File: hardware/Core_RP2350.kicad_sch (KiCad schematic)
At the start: 79 parts, among them J19 Micro_SD_Card_Det_Hirose_DM3AT, J20 USB_C_Receptacle_USB2.0, J21 5-146281-3, J22 5-146281-3, J4 AudioJack3, SW1 SPST-NO, SW2 SPST-NO, SW3 SPST-NO, U1 RP2350B-QFN80, U2 ADUM4160, U3 W25Q128JVS

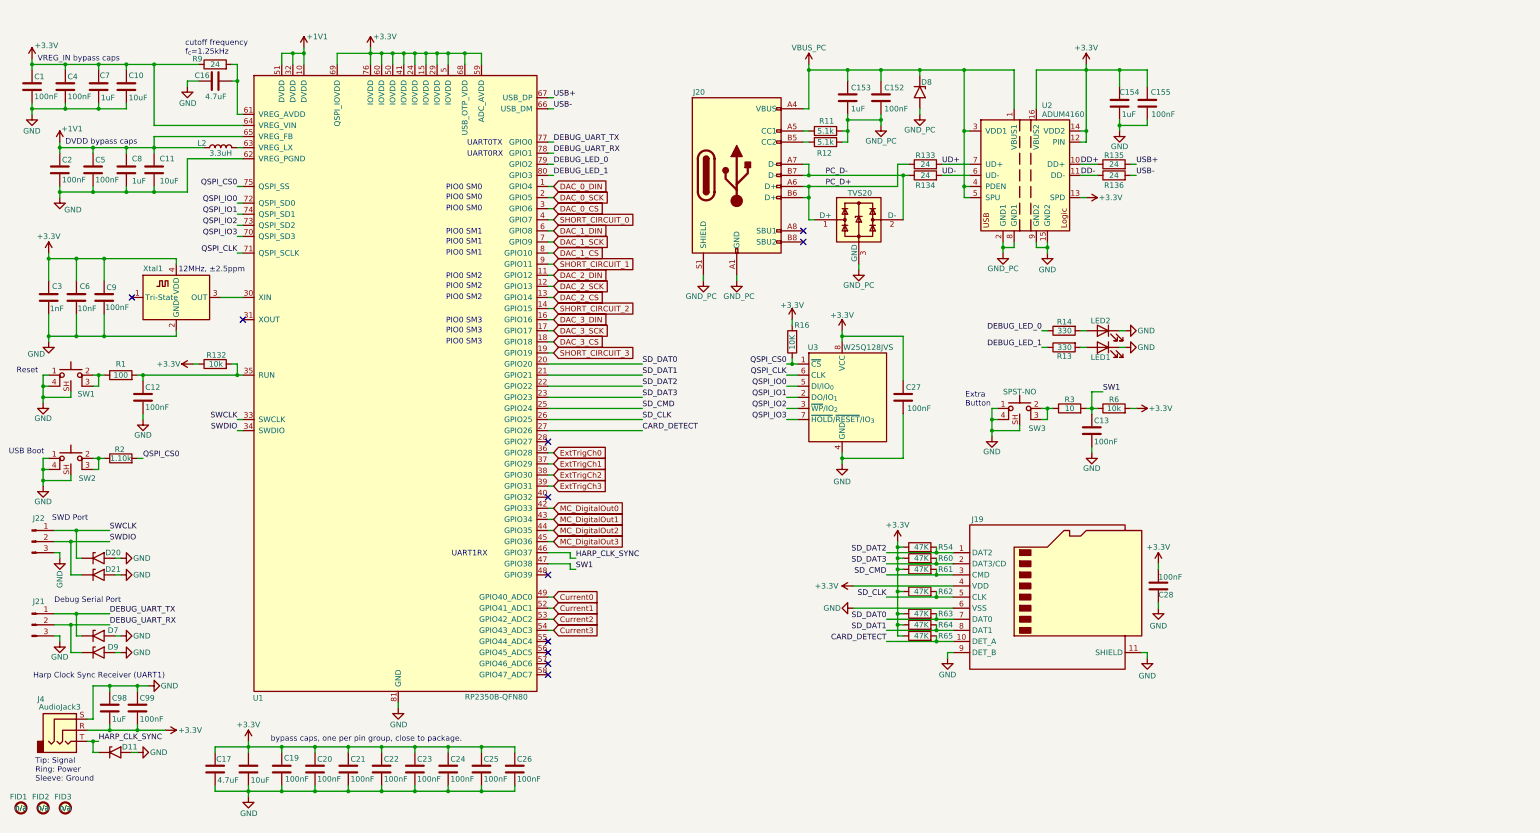
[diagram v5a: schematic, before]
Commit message: update short detection; draft bom
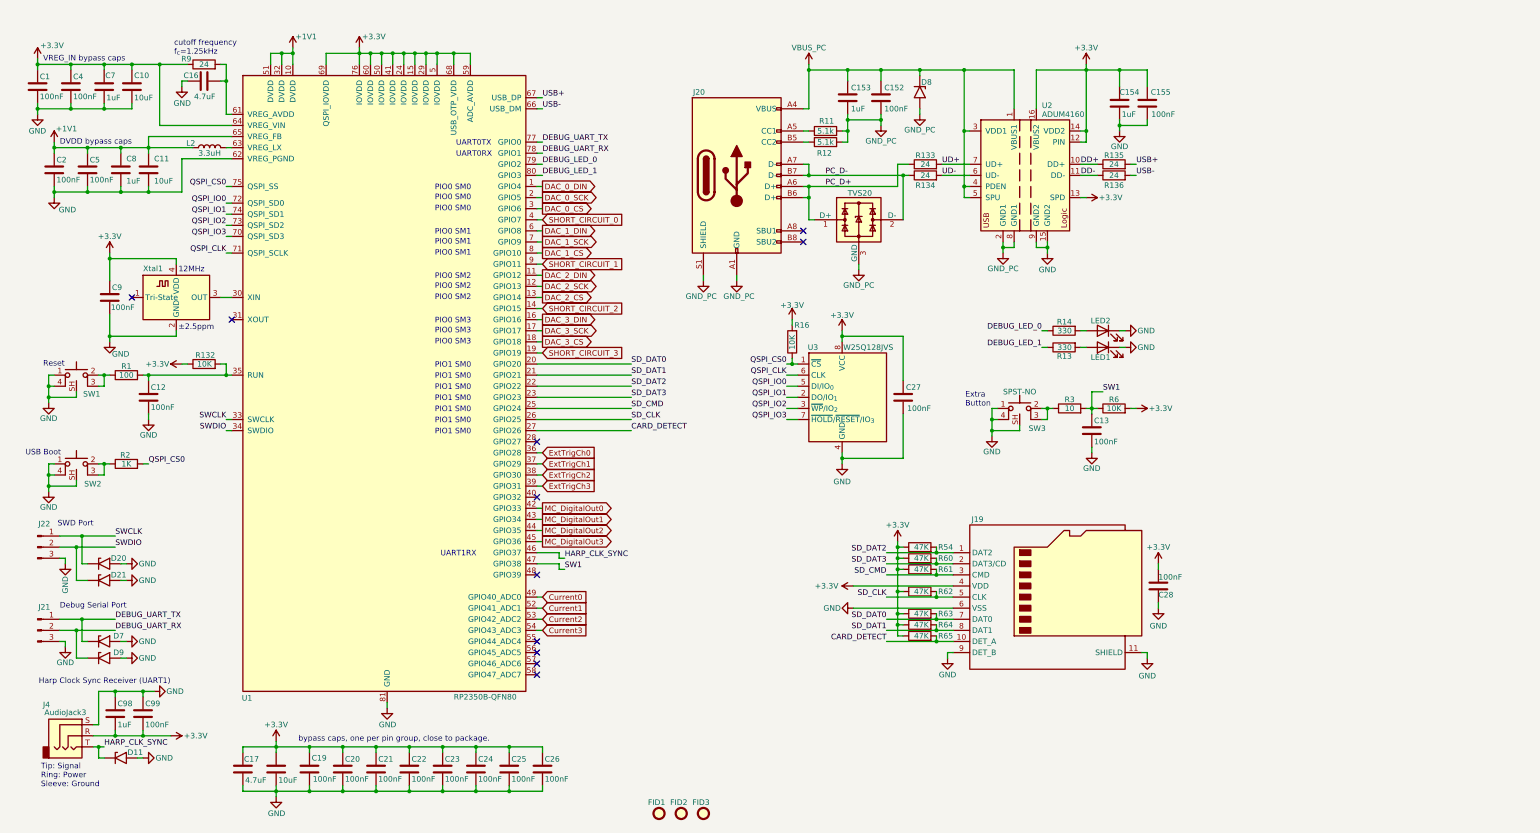
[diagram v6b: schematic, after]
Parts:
- removed C3: 1nF, Capacitor_SMD:C_0603_1608Metric, symbol harp.device.quad.dac:C_0603
- removed C6: 10nF, Capacitor_SMD:C_0603_1608Metric, symbol harp.device.quad.dac:C_0603
- C1, C12, C13, C152, C155, C19, C2, C20, C21, C22, C23, C24, C25, C26, C27, C28, C4, C5, C9, C99: footprint Capacitor_SMD:C_0603_1608Metric -> Capacitor_SMD:C_0402_1005Metric; Link https://www.digikey.com/en/products/detail/kemet/C0603C104K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 -> https://www.digikey.com/en/products/detail/murata-electroni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; Manufacturer KEMET -> Murata Electronics; Manufacturer Number C0603C104K5RACTU -> GRM155R71H104KE14D; Manufacturer_Name KEMET -> (none); Manufacturer_Part_Number C0603C104K5RACTU -> (none); PCBWay Link https://www.pcbway.com/components/detail/0402B104K160CT/307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 -> (none); Temperature Coefficient (none) -> X7R
- C10, C11, C18: Alternate CL21B106KOQNNNE -> (none); Manufacturer_Name Murata Electronics -> (none); Manufacturer_Part_Number GRM188R61E106KA73D -> (none); Temperature Coefficient (none) -> X5R
- C153, C154, C7, C8, C98: Manufacturer_Name TDK -> (none); Manufacturer_Part_Number C1608X7R1H105K080AB -> (none)
- C16, C17: Manufacturer_Name TDK -> (none); Manufacturer_Part_Number C1608X5R1V475K080AC -> (none)
- D11, D20, D21, D7, D8, D9: Link (none) -> https://www.digikey.com/en/products/detail/vishay-general-s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; Manufacturer (none) -> Vishay General Semiconductor - Diodes Division; Manufacturer Number (none) -> VBUS05N1-HD1-G3-08
- FID1, FID2, FID3: Manufacturer_Name n/a -> (none); Manufacturer_Part_Number n/a -> (none)
- J20: Manufacturer_Name JAE Electronics -> (none); Manufacturer_Part_Number DX07S016JA1R1500 -> (none); PCBWay Link https://www.pcbway.com/components/detail/DX07S016JA1R1500/1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 -> (none)
- J21, J22: Manufacturer_Name TE Connectivity -> (none); Manufacturer_Part_Number 5-146281-3 -> (none)
- J4: Manufacturer_Name Same Sky (Formerly CUI Devices) -> (none); Manufacturer_Part_Number SJ-3524-SMT-TR-BE -> (none)
- LED1, LED2: PCBWay Link https://www.pcbway.com/components/detail/XZCDGK53W1VF/50198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 -> (none)
- R1: Manufacturer_Name Yageo -> (none); Manufacturer_Part_Number AC0603FR-13100RL -> (none)
- R11, R12: footprint Resistor_SMD:R_0603_1608Metric -> Resistor_SMD:R_0402_1005Metric; Link https://www.digikey.com/en/products/detail/yageo/RC0603FR-0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 -> (none); Manufacturer Yageo -> (none); Manufacturer Number RT0402FRE075K1L -> (none); Manufacturer_Name Yageo -> (none); Manufacturer_Part_Number RC0603FR-075K1L -> (none); PCBWay Link https://www.pcbway.com/components/detail/RT0402FRE075K1L/44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 -> (none)
- R13, R14: Manufacturer_Name Yageo -> (none); Manufacturer_Part_Number RC0603FR-07330RL -> (none)
- R132: value 10k -> 10K; footprint Resistor_SMD:R_0603_1608Metric -> Resistor_SMD:R_0402_1005Metric; Link https://www.digikey.com/en/products/detail/yageo/RT0603BRD0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 -> (none); Manufacturer Yageo -> (none); Manufacturer Number RC0402FR-07680RL -> (none); Manufacturer_Name Yageo -> (none); Manufacturer_Part_Number RT0603BRD0710KL -> (none)
- R133, R134, R135, R136, R9: Manufacturer_Name Yageo -> (none); Manufacturer_Part_Number AC0603FR-0724RL -> (none)
- R16: footprint Resistor_SMD:R_0603_1608Metric -> Resistor_SMD:R_0402_1005Metric; Link https://www.digikey.com/en/products/detail/yageo/RT0603BRD0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 -> (none); Manufacturer Yageo -> (none); Manufacturer Number RT0402BRD071KL -> (none); Manufacturer_Name Yageo -> (none); Manufacturer_Part_Number RT0603BRD0710KL -> (none)
- R2: value 1.10k -> 1K; footprint Resistor_SMD:R_0603_1608Metric -> Resistor_SMD:R_0402_1005Metric; Link https://www.digikey.com/en/products/detail/yageo/RT0603BRD0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 -> (none); Manufacturer Yageo -> (none); Manufacturer Number RC0402FR-07680RL -> (none); Manufacturer_Name Yageo -> (none); Manufacturer_Part_Number RT0603BRD071K1L -> (none)
- R3: footprint Resistor_SMD:R_0603_1608Metric -> Resistor_SMD:R_0402_1005Metric; Manufacturer Yageo -> (none); Manufacturer Number RT0402BRD071KL -> (none); Manufacturer_Name Yageo -> (none); Manufacturer_Part_Number AC0603FR-1310RL -> (none)
- R54, R60, R61, R62, R63, R64, R65: footprint (none) -> Resistor_SMD:R_0402_1005Metric
- R6: value 10k -> 10K; footprint Resistor_SMD:R_0603_1608Metric -> Resistor_SMD:R_0402_1005Metric; Link https://www.digikey.com/en/products/detail/yageo/RT0603BRD0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 -> (none); Manufacturer Yageo -> (none); Manufacturer Number RT0402BRD071KL -> (none); Manufacturer_Name Yageo -> (none); Manufacturer_Part_Number RT0603BRD0710KL -> (none)
- SW1, SW2, SW3: Manufacturer_Name Würth Elektronik -> (none); Manufacturer_Part_Number 435451019820 -> (none); Supplier Link https://www.digikey.com/en/products/detail/w%C3%BCrth-elekt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 -> (none)
- TVS20: Manufacturer_Name Texas Instruments -> (none); Manufacturer_Part_Number TPD2EUSB30DRTR -> (none); PCBWay Link https://www.pcbway.com/components/detail/TPD2EUSB30ADRTR/32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 -> (none)
- U1: Manufacturer_Name Raspberry Pi -> (none); Manufacturer_Part_Number SC1510-A4 -> (none); Supplier Link https://www.digikey.com/en/products/detail/raspberry-pi/SC1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 -> (none)
- U2: Manufacturer_Name Analog Devices -> (none); Manufacturer_Part_Number ADUM4160BRWZ-RL -> (none); PCBWay Link https://www.pcbway.com/components/detail/ADUM4160BRWZRL/328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 -> (none)
- U3: Manufacturer_Name Winbond Electronics -> (none); Manufacturer_Part_Number W25Q128JVSIQ TR -> (none)
- Xtal1: Manufacturer_Name ECS -> (none); Manufacturer_Part_Number ECS-TXO-2016-33-120-TR -> (none); PCBWay Link https://www.pcbway.com/components/detail/ECSTXO201633120TR/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 -> (none); Supplier Link https://www.digikey.com/en/products/detail/ecs-inc/ECS-TXO-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 -> (none)
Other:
- note added: "12MHz"
- note added: "PIO1 SM0"
- note added: "±2.5ppm"
- note removed: "12MHz, ±2.5ppm"
- moved on the sheet: C1, C10, C11, C12, C16, C17, C19, C2, C20, C21, C22, C23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

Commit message: update board draft
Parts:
- removed C10, C11: 10uF, Capacitor_SMD:C_0603_1608Metric, symbol harp.device.quad.dac:C_0603
- removed C4, C5: 100nF, Capacitor_SMD:C_0402_1005Metric, symbol harp.device.quad.dac:C_0603
- removed C7, C8: 1uF, Capacitor_SMD:C_0603_1608Metric, symbol harp.device.quad.dac:C_0603
- removed U1: RP2350B-QFN80, harp.device.quad.dac.kicad:RP2350B_QFN-80_EP_10.573x10.573_Pitch0.4mm, symbol harp.device.quad.dac:RP2350B-QFN80
- added U32: RP2350_80QFN, kicad-lib:RP2350-QFN-80-1EP_10x10_P0.4mm_EP3.4x3.4mm_ThermalVias, symbol kicad-lib:RP2350_80QFN
- C1, C2: value 100nF -> 4.7uF; footprint Capacitor_SMD:C_0402_1005Metric -> Capacitor_SMD:C_0603_1608Metric; Alternate (none) -> CL21B106KOQNNNE; Link https://www.digikey.com/en/products/detail/murata-electroni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 -> https://www.digikey.com/en/products/detail/tdk-corporation/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; Manufacturer Murata Electronics -> TDK; Manufacturer Number GRM155R71H104KE14D -> C1608X5R1V475K080AC; Rated Voltage 50V -> 35V; Temperature Coefficient X7R -> (none)
- J1: renamed from J22; footprint harp.device.quad.dac.kicad:PinHeader_1x03_P2.54mm_Vertical -> Connector_PinHeader_2.54mm:PinHeader_1x03_P2.54mm_Vertical
- J2: renamed from J21; footprint harp.device.quad.dac.kicad:PinHeader_1x03_P2.54mm_Vertical -> Connector_PinHeader_2.54mm:PinHeader_1x03_P2.54mm_Vertical
- J3: renamed from J4; footprint harp.device.quad.dac.kicad:Jack_3.5mm_CUI_SJ-3524-SMT_Horizontal -> Connector_Audio:Jack_3.5mm_CUI_SJ-3524-SMT_Horizontal
- J4: renamed from J20; footprint harp.device.quad.dac.kicad:USB_C_Receptacle_JAE_DX07S016JA1R1500 -> Connector_USB:USB_C_Receptacle_JAE_DX07S016JA1R1500
- SW1, SW2, SW3: footprint harp.device.quad.dac.kicad:SW_Push_1P1T-SH_NO_Vertical_Wuerth_WS-TASV -> kicad-lib:SW_Push_1P1T-SH_NO_Vertical_Wuerth_WS-TASV
- U2: renamed from U3; value W25Q128JVS -> W25Q16JVUXIQ; footprint harp.device.quad.dac.kicad:SOIC-8_5.3x5.3mm_P1.27mm -> Package_SON:Winbond_USON-8-1EP_3x2mm_P0.5mm_EP0.2x1.6mm; Link https://www.digikey.com/en/products/detail/winbond-electronics/W25Q128JVSIQ-TR/5803944 -> https://www.digikey.com/en/products/detail/winbond-electronics/W25Q16JVUXIQ-TR/15182017; Manufacturer Number (none) -> W25Q16JVUXIQ TR
- U3: renamed from U2; footprint harp.device.quad.dac.kicad:SOIC-16W_7.5x10.3mm_P1.27mm -> Package_SO:SOIC-16W_7.5x10.3mm_P1.27mm
- Xtal1: footprint harp.device.quad.dac.kicad:Crystal_SMD_2016-4Pin_2.0x1.6mm -> Crystal:Crystal_SMD_2016-4Pin_2.0x1.6mm; symbol harp.device.quad.dac:ECS-TXO-2016 -> kicad-lib:ECS-TXO-2016
- renumbered C99 to C10, C16 to C13, C17 to C14, C18 to C15, C19 to C16, C20 to C17, C21 to C18, C22 to C19, C23 to C20, C24 to C21, C25 to C22, C26 to C23, C153 to C24, C152 to C25, C27 to C26, C13 to C27, C154 to C28, C155 to C29, C28 to C30, C9 to C6, C98 to C7, D20 to D1, D21 to D2, D7 to D3, D9 to D4, D11 to D5, D8 to D6, J19 to J5, L2 to L1, LED2 to LED1, LED1 to LED2, R61 to R10, R62 to R11, R63 to R12, R64 to R13, R65 to R14, R133 to R15, R134 to R16, R14 to R17, R13 to R18, R3 to R19, R135 to R20, R136 to R21, R6 to R22, R9 to R3, R132 to R4, R16 to R5, R11 to R6, R12 to R7, R54 to R8, R60 to R9, TVS20 to TVS1
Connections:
- net +1V1: now also C1.1, U32.10 (DVDD), U32.32 (DVDD), U32.51 (DVDD), U32.65 (VREG_FB); no longer C2.2
- net +3.3V: now also C2.1, U32.15 (IOVDD), U32.24 (IOVDD), U32.29 (IOVDD), U32.41 (IOVDD), U32.5 (IOVDD), U32.50 (IOVDD), U32.59 (ADC_AVDD), U32.60 (IOVDD), U32.64 (VREG_VIN), U32.68 (USB_OTP_VDD), U32.69 (QSPI_IOVDD), U32.76 (IOVDD); no longer C1.2
- net CARD_DETECT: now also U32.28 (GPIO27)
- net Current0: now also U32.49 (GPIO40_ADC0)
- net Current1: now also U32.52 (GPIO41_ADC1)
- net Current2: now also U32.53 (GPIO42_ADC2)
- net Current3: now also U32.54 (GPIO43_ADC3)
- net DAC_0_CS: now also U32.3 (GPIO6)
- net DAC_0_DIN: now also U32.1 (GPIO4)
- net DAC_0_SCK: now also U32.2 (GPIO5)
- net DAC_1_CS: now also U32.8 (GPIO10)
- net DAC_1_DIN: now also U32.6 (GPIO8)
- net DAC_1_SCK: now also U32.7 (GPIO9)
- net DAC_2_CS: now also U32.13 (GPIO14)
- net DAC_2_DIN: now also U32.11 (GPIO12)
- net DAC_2_SCK: now also U32.12 (GPIO13)
- net DAC_3_CS: now also U32.18 (GPIO18)
- net DAC_3_DIN: now also U32.16 (GPIO16)
- net DAC_3_SCK: now also U32.17 (GPIO17)
- net DEBUG_LED_0: now also U32.79 (GPIO2)
- net DEBUG_LED_1: now also U32.80 (GPIO3)
- net DEBUG_UART_RX: now also U32.78 (GPIO1)
- net DEBUG_UART_TX: now also U32.77 (GPIO0)
- net ExtTrigCh0: now also U32.37 (GPIO29)
- net ExtTrigCh1: now also U32.38 (GPIO30)
- net ExtTrigCh2: now also U32.39 (GPIO31)
- net ExtTrigCh3: now also U32.40 (GPIO32)
- net GND: now also C1.2, C2.2, U32.62 (VREG_PGND), U32.81 (GND); no longer C1.1, C2.1
- net HARP_CLK_SYNC: now also U32.46 (GPIO37)
- net MC_DigitalOut0: now also U32.42 (GPIO33)
- net MC_DigitalOut1: now also U32.43 (GPIO34)
- net MC_DigitalOut2: now also U32.44 (GPIO35)
- net MC_DigitalOut3: now also U32.45 (GPIO36)
- net QSPI_CLK: now also U32.71 (QSPI_SCLK)
- net QSPI_CS0: now also U32.75 (QSPI_SS)
- net QSPI_IO0: now also U32.72 (QSPI_SD0)
- net QSPI_IO1: now also U32.74 (QSPI_SD1)
- net QSPI_IO2: now also U32.73 (QSPI_SD2)
- net QSPI_IO3: now also U32.70 (QSPI_SD3)
- net SD_CLK: now also U32.27 (GPIO26)
- net SD_CMD: now also U32.26 (GPIO25)
- net SD_DAT0: now also U32.21 (GPIO21)
- net SD_DAT1: now also U32.22 (GPIO22)
- net SD_DAT2: now also U32.23 (GPIO23)
- net SD_DAT3: now also U32.25 (GPIO24)
- net SHORT_CIRCUIT_0: now also U32.4 (GPIO7)
- net SHORT_CIRCUIT_1: now also U32.9 (GPIO11)
- net SHORT_CIRCUIT_2: now also U32.14 (GPIO15)
- net SHORT_CIRCUIT_3: now also U32.19 (GPIO19)
- net SW1: now also U32.47 (GPIO38)
- net SWCLK: now also U32.33 (SWCLK)
- net SWDIO: now also U32.34 (SWD)
- net USB+: now also U32.67 (USB_DP)
- net USB-: now also U32.66 (USB_DM)
- net at C12.2, R1.2, R4.2: now also U32.35 (RUN)
- net at C13.2, R3.2: now also U32.61 (VREG_AVDD)
- net at L1.2: now also U32.63 (VREG_LX)
- net at Xtal1.3 (OUT): now also U32.30 (XIN)
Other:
- note removed: "DVDD bypass caps"
- note removed: "VREG_IN bypass caps"
- moved on the sheet: C10, C12, C13, C6, C7, D1, D2, D3, D4, D5, J1, J2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
